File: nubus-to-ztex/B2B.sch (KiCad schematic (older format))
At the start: 14 parts, among them J1 Conn_02x07_Odd_Even, J2 Conn_01x06_Male, J8 Conn_02x07_Odd_Even

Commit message: large update
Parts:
- added C4: 100nF, Capacitor_SMD:C_0603_1608Metric, symbol Device:C
- J1: Datasheet-ALT (none) -> https://datasheet.lcsc.com/lcsc/1811051309_MOLEX-878311420_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; Notes (none) -> 87831-1419, 87831-1420, 87831-1421, 87831-1436 only change 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
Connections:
- net +3V3: now also C4.1
- net GND: now also C4.2
- net ~NMRQ_3V3: no longer JAB1.6 (J18~IO_L23N_T3_FWE_B_15)
- net fpga_to_cpld_signal_2: no longer names the net of JAB1.16 (G14~IO_L15N_T2_DQS_ADV_B_15)
- new net NMRQ: JAB1.6 (J18~IO_L23N_T3_FWE_B_15)
- no-connect marks 4 -> 5
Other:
- note added: "User LEDS"
- note added: "design use NMRQ (active high) instead"
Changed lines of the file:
@@
 F 7 "87831-1420" H 3150 7250 50  0001 C CNN "MPN"
 F 8 "https://www2.mouser.com/ProductDetail/Molex/87831-1420?qs=QtQX4uD3c2VDCL534TqpVg%3D%3D" H 3150 7250 50  0001 C CNN "URL"
+F 9 "https://datasheet.lcsc.com/lcsc/1811051309_MOLEX-878311420_C240854.pdf" H 3150 7250 50  0001 C CNN "Datasheet-ALT"
+F 10 "87831-1419, 87831-1420, 87831-1421, 87831-1436 only change plating" H 3150 7250 50  0001 C CNN "Notes"
 	1    3150 7250
 	1    0    0    -1
@@
 Text GLabel 1600 1350 0    50   Input ~ 0
 ~RQST_3V3
-Text GLabel 4100 1350 2    50   Input ~ 0
+Text GLabel 4750 650  2    50   Input ~ 0
 ~NMRQ_3V3
 Text GLabel 1600 1550 0    50   Input ~ 0
@@
 AR Path="/618E8C75/61B5DFCC" Ref="D2"  Part="1"
 F 0 "D2" H 1000 6000 50  0000 C CNN
-F 1 "RED" H 650 5900 50  0000 R CNN
+F 1 "RED" H 1050 5750 50  0000 R CNN
 F 2 "LED_SMD:LED_0805_2012Metric" H 1000 5900 50  0001 C CNN
 F 3 "https://optoelectronics.liteon.com/upload/download/DS-22-99-0150/LTST-C170KRKT.pdf" H 1000 5900 50  0001 C CNN
@@
 AR Path="/618E8C75/61B5F405" Ref="D3"  Part="1"
 F 0 "D3" H 1000 6500 50  0000 C CNN
-F 1 "RED" H 650 6400 50  0000 R CNN
+F 1 "RED" H 1050 6250 50  0000 R CNN
 F 2 "LED_SMD:LED_0805_2012Metric" H 1000 6400 50  0001 C CNN
 F 3 "https://optoelectronics.liteon.com/upload/download/DS-22-99-0150/LTST-C170KRKT.pdf" H 1000 6400 50  0001 C CNN
@@
 AR Path="/618E8C75/61B60A6F" Ref="D4"  Part="1"
 F 0 "D4" H 1000 7000 50  0000 C CNN
-F 1 "RED" H 650 6900 50  0000 R CNN
+F 1 "RED" H 1050 6750 50  0000 R CNN
 F 2 "LED_SMD:LED_0805_2012Metric" H 1000 6900 50  0001 C CNN
 F 3 "https://optoelectronics.liteon.com/upload/download/DS-22-99-0150/LTST-C170KRKT.pdf" H 1000 6900 50  0001 C CNN
@@
 AR Path="/618E8C75/61B62362" Ref="D5"  Part="1"
 F 0 "D5" H 1000 7500 50  0000 C CNN
-F 1 "RED" H 650 7400 50  0000 R CNN
+F 1 "RED" H 1050 7250 50  0000 R CNN
 F 2 "LED_SMD:LED_0805_2012Metric" H 1000 7400 50  0001 C CNN
 F 3 "https://optoelectronics.liteon.com/upload/download/DS-22-99-0150/LTST-C170KRKT.pdf" H 1000 7400 50  0001 C CNN
@@
 Text GLabel 7400 1650 0    39   Input ~ 8
 tmoen
-Text GLabel 4100 1850 2    39   Input ~ 8
-fpga_to_cpld_signal_2
 Text GLabel 1600 1750 0    39   Input ~ 8
 fpga_to_cpld_signal
+$Comp
+L Device:C C?
+U 1 1 61F08531
+P 2750 6050
+AR Path="/618F532C/61F08531" Ref="C?"  Part="1"
+AR Path="/618E8C75/61F08531" Ref="C4"  Part="1"
+F 0 "C4" H 2775 6150 50  0000 L CNN
+F 1 "100nF" H 2775 5950 50  0000 L CNN
+F 2 "Capacitor_SMD:C_0603_1608Metric" H 2788 5900 50  0001 C CNN
+F 3 "" H 2750 6050 50  0000 C CNN
+F 4 "www.yageo.com" H 2750 6050 50  0001 C CNN "MNF1_URL"
+F 5 "CC0603KRX7R8BB104" H 2750 6050 50  0001 C CNN "MPN"
+F 6 "603-CC603KRX7R8BB104" H 2750 6050 50  0001 C CNN "Mouser"
+F 7 "?" H 2750 6050 50  0001 C CNN "Digikey"
+F 8 "?" H 2750 6050 50  0001 C CNN "LCSC"
+F 9 "?" H 2750 6050 50  0001 C CNN "Koncar"
+F 10 "TB" H 2750 6050 50  0001 C CNN "Side"
+	1    2750 6050
+	1    0    0    -1
+$EndComp
+$Comp
+L power:GND #PWR0132
+U 1 1 61F08538
+P 2750 6200
+F 0 "#PWR0132" H 2750 5950 50  0001 C CNN
+F 1 "GND" H 2755 6027 50  0000 C CNN
+F 2 "" H 2750 6200 50  0001 C CNN
+F 3 "" H 2750 6200 50  0001 C CNN
+	1    2750 6200
+	1    0    0    -1
+$EndComp
+$Comp
+L power:+3.3V #PWR0133
+U 1 1 61F0853E
+P 2750 5900
+F 0 "#PWR0133" H 2750 5750 50  0001 C CNN
+F 1 "+3.3V" H 2765 6073 50  0000 C CNN
+F 2 "" H 2750 5900 50  0001 C CNN
+F 3 "" H 2750 5900 50  0001 C CNN
+	1    2750 5900
+	1    0    0    -1
+$EndComp
+Text Notes 1200 5650 0    50   ~ 0
+User LEDS
+Text GLabel 4100 1350 2    50   Input ~ 0
+NMRQ
+Text Notes 5700 550  2    50   ~ 0
+design use NMRQ (active high) instead
+NoConn ~ 4750 650
 $EndSCHEMATC

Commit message: another update after discussion on tinkerdifferent
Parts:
- removed D4, D5: RED, LED_SMD:LED_0805_2012Metric, symbol Device:LED_ALT
- removed R10, R9: 549, Resistor_SMD:R_0603_1608Metric, symbol Device:R
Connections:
- net NMRQ is gone; now on net ~NMRQ_3V3: JAB1.6 (J18~IO_L23N_T3_FWE_B_15)
- net LED2: no longer JCD1.16 (T5~IO_L12P_T1_MRCC_34)
- net LED3: no longer JCD1.18 (T4~IO_L12N_T1_MRCC_34)
- net fpga_to_cpld_signal_2: now reaches JAB1.16 (G14~IO_L15N_T2_DQS_ADV_B_15)
- new net ~CLK2X_3V3: JCD1.16 (T5~IO_L12P_T1_MRCC_34)
- new net ~TM2_3V3: JCD1.18 (T4~IO_L12N_T1_MRCC_34)
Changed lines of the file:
@@
 Text GLabel 1850 6400 2    60   Input ~ 12
 LED1
-Wire Wire Line
-	850  6900 700  6900
-Wire Wire Line
-	700  6900 700  7100
-Wire Wire Line
-	1150 6900 1550 6900
-$Comp
-L Device:R R?
-U 1 1 61B60A5F
-P 1700 6900
-AR Path="/5F6B165A/61B60A5F" Ref="R?"  Part="1"
-AR Path="/5F67E4B9/61B60A5F" Ref="R?"  Part="1"
-AR Path="/618E8C75/61B60A5F" Ref="R9"  Part="1"
-F 0 "R9" V 1780 6900 50  0000 C CNN
-F 1 "549" V 1700 6900 50  0000 C CNN
-F 2 "Resistor_SMD:R_0603_1608Metric" V 1630 6900 50  0001 C CNN
-F 3 "" H 1700 6900 50  0000 C CNN
-F 4 "0603WAF5490T5E" V 1700 6900 50  0001 C CNN "MPN"
-F 5 "https://lcsc.com/product-detail/Chip-Resistor-Surface-Mount_UNI-ROYAL-Uniroyal-Elec-0603WAF5490T5E_C23079.html" V 1700 6900 50  0001 C CNN "URL"
-	1    1700 6900
-	0    1    1    0
-$EndComp
-$Comp
-L Device:LED_ALT D?
-U 1 1 61B60A6F
-P 1000 6900
-AR Path="/5F6B165A/61B60A6F" Ref="D?"  Part="1"
-AR Path="/5F67E4B9/61B60A6F" Ref="D?"  Part="1"
-AR Path="/618E8C75/61B60A6F" Ref="D4"  Part="1"
-F 0 "D4" H 1000 7000 50  0000 C CNN
-F 1 "RED" H 1050 6750 50  0000 R CNN
-F 2 "LED_SMD:LED_0805_2012Metric" H 1000 6900 50  0001 C CNN
-F 3 "https://optoelectronics.liteon.com/upload/download/DS-22-99-0150/LTST-C170KRKT.pdf" H 1000 6900 50  0001 C CNN
-F 4 "www.liteon.com" H 1000 6900 60  0001 C CNN "MNF1_URL"
-F 5 "LTST-C170KRKT" H 1000 6900 60  0001 C CNN "MPN"
-F 6 "https://www.lcsc.com/product-detail/Light-Emitting-Diodes-LED_Lite-On-LTST-C170KRKT_C94868.html" H 1000 6900 50  0001 C CNN "URL"
-	1    1000 6900
-	1    0    0    -1
-$EndComp
-$Comp
-L power:GND #PWR0177
-U 1 1 61B60A76
-P 700 7100
-F 0 "#PWR0177" H 700 6850 50  0001 C CNN
-F 1 "GND" H 705 6927 50  0000 C CNN
-F 2 "" H 700 7100 50  0001 C CNN
-F 3 "" H 700 7100 50  0001 C CNN
-	1    700  7100
-	1    0    0    -1
-$EndComp
-Text GLabel 1850 6900 2    60   Input ~ 12
-LED2
-Wire Wire Line
-	850  7400 700  7400
-Wire Wire Line
-	700  7400 700  7600
-Wire Wire Line
-	1150 7400 1550 7400
-$Comp
-L Device:R R?
-U 1 1 61B62352
-P 1700 7400
-AR Path="/5F6B165A/61B62352" Ref="R?"  Part="1"
-AR Path="/5F67E4B9/61B62352" Ref="R?"  Part="1"
-AR Path="/618E8C75/61B62352" Ref="R10"  Part="1"
-F 0 "R10" V 1780 7400 50  0000 C CNN
-F 1 "549" V 1700 7400 50  0000 C CNN
-F 2 "Resistor_SMD:R_0603_1608Metric" V 1630 7400 50  0001 C CNN
-F 3 "" H 1700 7400 50  0000 C CNN
-F 4 "0603WAF5490T5E" V 1700 7400 50  0001 C CNN "MPN"
-F 5 "https://lcsc.com/product-detail/Chip-Resistor-Surface-Mount_UNI-ROYAL-Uniroyal-Elec-0603WAF5490T5E_C23079.html" V 1700 7400 50  0001 C CNN "URL"
-	1    1700 7400
-	0    1    1    0
-$EndComp
-$Comp
-L Device:LED_ALT D?
-U 1 1 61B62362
-P 1000 7400
-AR Path="/5F6B165A/61B62362" Ref="D?"  Part="1"
-AR Path="/5F67E4B9/61B62362" Ref="D?"  Part="1"
-AR Path="/618E8C75/61B62362" Ref="D5"  Part="1"
-F 0 "D5" H 1000 7500 50  0000 C CNN
-F 1 "RED" H 1050 7250 50  0000 R CNN
-F 2 "LED_SMD:LED_0805_2012Metric" H 1000 7400 50  0001 C CNN
-F 3 "https://optoelectronics.liteon.com/upload/download/DS-22-99-0150/LTST-C170KRKT.pdf" H 1000 7400 50  0001 C CNN
-F 4 "www.liteon.com" H 1000 7400 60  0001 C CNN "MNF1_URL"
-F 5 "LTST-C170KRKT" H 1000 7400 60  0001 C CNN "MPN"
-F 6 "https://www.lcsc.com/product-detail/Light-Emitting-Diodes-LED_Lite-On-LTST-C170KRKT_C94868.html" H 1000 7400 50  0001 C CNN "URL"
-	1    1000 7400
-	1    0    0    -1
-$EndComp
-$Comp
-L power:GND #PWR0178
-U 1 1 61B62369
-P 700 7600
-F 0 "#PWR0178" H 700 7350 50  0001 C CNN
-F 1 "GND" H 705 7427 50  0000 C CNN
-F 2 "" H 700 7600 50  0001 C CNN
-F 3 "" H 700 7600 50  0001 C CNN
-	1    700  7600
-	1    0    0    -1
-$EndComp
-Text GLabel 1850 7400 2    60   Input ~ 12
-LED3
 Text GLabel 9900 1650 2    60   Input ~ 12
 LED0
 Text GLabel 9900 1750 2    60   Input ~ 12
 LED1
-Text GLabel 9900 1850 2    60   Input ~ 12
-LED2
-Text GLabel 9900 1950 2    60   Input ~ 12
-LED3
 Text GLabel 1600 4050 0    50   Input ~ 0
 USBH0_D+
@@
 User LEDS
 Text GLabel 4100 1350 2    50   Input ~ 0
-NMRQ
+~NMRQ_3V3
 Text Notes 5700 550  2    50   ~ 0
 design use NMRQ (active high) instead
 NoConn ~ 4750 650
+Text GLabel 4100 1850 2    39   Input ~ 8
+fpga_to_cpld_signal_2
+Text GLabel 12450 1800 2    60   Input ~ 12
+LED3
+Text GLabel 12450 1700 2    60   Input ~ 12
+LED2
+Text GLabel 9900 1950 2    50   Input ~ 0
+~TM2_3V3
+Text GLabel 9900 1850 2    50   Input ~ 0
+~CLK2X_3V3
 $EndSCHEMATC

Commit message: large clean-up update
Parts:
- added C3: 47uF 10V+, Capacitor_SMD:C_0805_2012Metric, symbol Device:C
- added D3: BLUE, LED_SMD:LED_0805_2012Metric, symbol Device:LED_ALT
- added R3: 549, Resistor_SMD:R_0603_1608Metric, symbol Device:R
- renumbered C19 to C1, C4 to C2, D2 to D1, D3 to D2, J8 to J2, J2 to J3, R7 to R1, R8 to R2
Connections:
- net +3V3: now also R3.1
- net +5V: now also C3.1
- net GND: now also C3.2, D3.1 (K)
- new net: D3.2 (A), R3.2
- no-connect marks 5 -> 4
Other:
- note added: "Close to VIN\npins on AB"
- note added: "Close to pwr output pins\n(3.3V / VCCO_{AB,CD})"
- note added: "Power Signal"
- note added: "Serial port-like header\n(just two signals & gnd, really)"
- note removed: "design use NMRQ (active high) instead"
- moved on the sheet: C1, C2

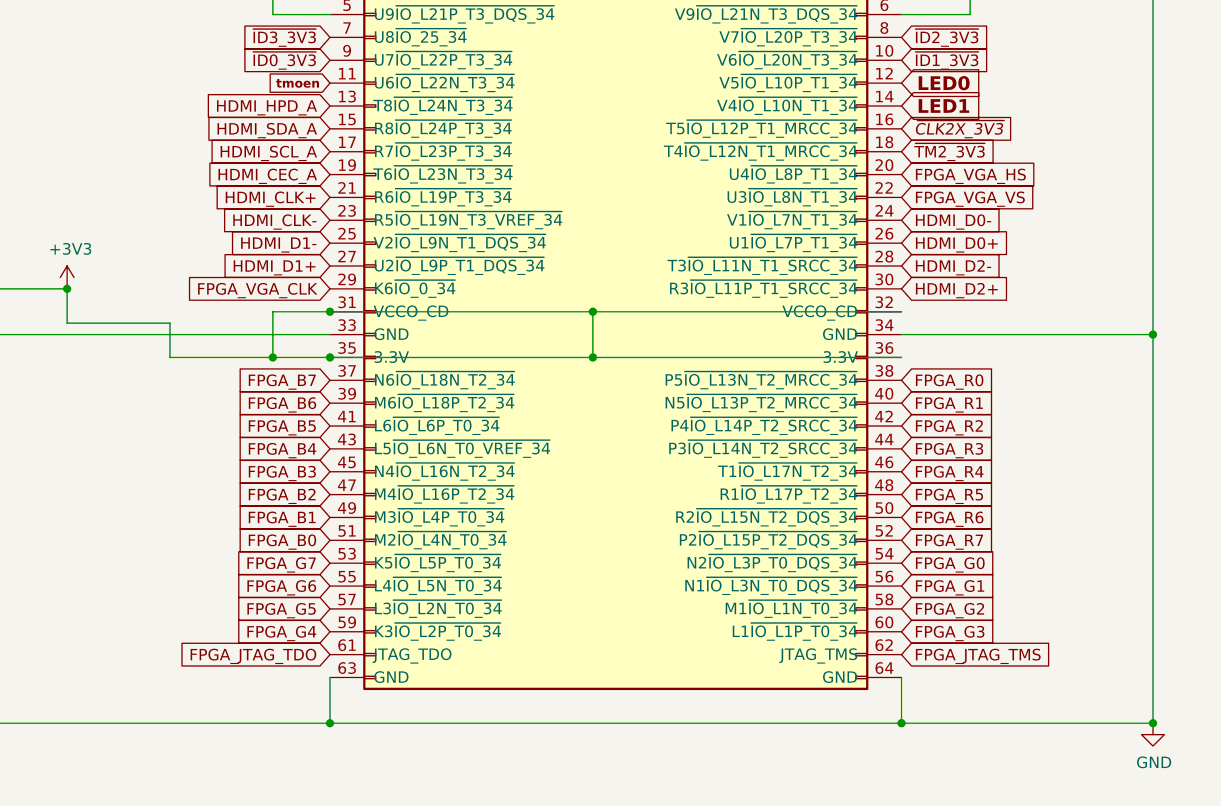
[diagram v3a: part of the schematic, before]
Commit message: drop vga
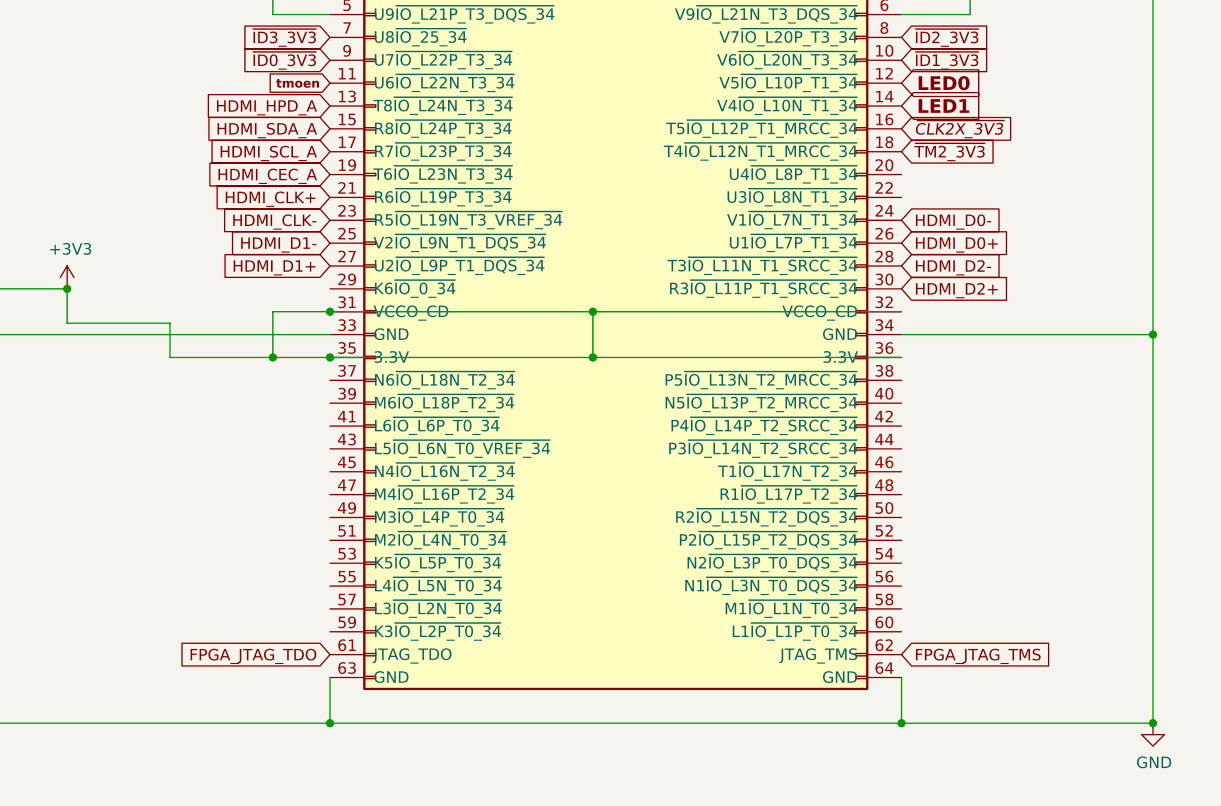
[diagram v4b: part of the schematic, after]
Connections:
- net FPGA_B0: no longer names the net of JCD1.51 (M2~IO_L4N_T0_34)
- net FPGA_B1: no longer names the net of JCD1.49 (M3~IO_L4P_T0_34)
- net FPGA_B2: no longer names the net of JCD1.47 (M4~IO_L16P_T2_34)
- net FPGA_B3: no longer names the net of JCD1.45 (N4~IO_L16N_T2_34)
- net FPGA_B4: no longer names the net of JCD1.43 (L5~IO_L6N_T0_VREF_34)
- net FPGA_B5: no longer names the net of JCD1.41 (L6~IO_L6P_T0_34)
- net FPGA_B6: no longer names the net of JCD1.39 (M6~IO_L18P_T2_34)
- net FPGA_B7: no longer names the net of JCD1.37 (N6~IO_L18N_T2_34)
- net FPGA_G0: no longer names the net of JCD1.54 (N2~IO_L3P_T0_DQS_34)
- net FPGA_G1: no longer names the net of JCD1.56 (N1~IO_L3N_T0_DQS_34)
- net FPGA_G2: no longer names the net of JCD1.58 (M1~IO_L1N_T0_34)
- net FPGA_G3: no longer names the net of JCD1.60 (L1~IO_L1P_T0_34)
- net FPGA_G4: no longer names the net of JCD1.59 (K3~IO_L2P_T0_34)
- net FPGA_G5: no longer names the net of JCD1.57 (L3~IO_L2N_T0_34)
- net FPGA_G6: no longer names the net of JCD1.55 (L4~IO_L5N_T0_34)
- net FPGA_G7: no longer names the net of JCD1.53 (K5~IO_L5P_T0_34)
- net FPGA_R0: no longer names the net of JCD1.38 (P5~IO_L13N_T2_MRCC_34)
- net FPGA_R1: no longer names the net of JCD1.40 (N5~IO_L13P_T2_MRCC_34)
- net FPGA_R2: no longer names the net of JCD1.42 (P4~IO_L14P_T2_SRCC_34)
- net FPGA_R3: no longer names the net of JCD1.44 (P3~IO_L14N_T2_SRCC_34)
- net FPGA_R4: no longer names the net of JCD1.46 (T1~IO_L17N_T2_34)
- net FPGA_R5: no longer names the net of JCD1.48 (R1~IO_L17P_T2_34)
- net FPGA_R6: no longer names the net of JCD1.50 (R2~IO_L15N_T2_DQS_34)
- net FPGA_R7: no longer names the net of JCD1.52 (P2~IO_L15P_T2_DQS_34)
- net FPGA_VGA_CLK: no longer names the net of JCD1.29 (K6~IO_0_34)
- net FPGA_VGA_HS: no longer names the net of JCD1.20 (U4~IO_L8P_T1_34)
- net FPGA_VGA_VS: no longer names the net of JCD1.22 (U3~IO_L8N_T1_34)
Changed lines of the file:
@@
 Text GLabel 1600 2450 0    39   Input ~ 8
 NUBUS_OE
-Text GLabel 9900 2950 2    50   Input ~ 0
-FPGA_R0
-Text GLabel 9900 3050 2    50   Input ~ 0
-FPGA_R1
-Text GLabel 9900 3150 2    50   Input ~ 0
-FPGA_R2
-Text GLabel 9900 3250 2    50   Input ~ 0
-FPGA_R3
-Text GLabel 9900 3350 2    50   Input ~ 0
-FPGA_R4
-Text GLabel 9900 3450 2    50   Input ~ 0
-FPGA_R5
-Text GLabel 9900 3550 2    50   Input ~ 0
-FPGA_R6
-Text GLabel 9900 3650 2    50   Input ~ 0
-FPGA_R7
-Text GLabel 9900 3750 2    50   Input ~ 0
-FPGA_G0
-Text GLabel 9900 3850 2    50   Input ~ 0
-FPGA_G1
-Text GLabel 9900 3950 2    50   Input ~ 0
-FPGA_G2
-Text GLabel 9900 4050 2    50   Input ~ 0
-FPGA_G3
-Text GLabel 7400 4050 0    50   Input ~ 0
-FPGA_G4
-Text GLabel 7400 3950 0    50   Input ~ 0
-FPGA_G5
-Text GLabel 7400 3850 0    50   Input ~ 0
-FPGA_G6
-Text GLabel 7400 3750 0    50   Input ~ 0
-FPGA_G7
-Text GLabel 7400 3650 0    50   Input ~ 0
-FPGA_B0
-Text GLabel 7400 3550 0    50   Input ~ 0
-FPGA_B1
-Text GLabel 7400 3450 0    50   Input ~ 0
-FPGA_B2
-Text GLabel 7400 3350 0    50   Input ~ 0
-FPGA_B3
-Text GLabel 7400 3250 0    50   Input ~ 0
-FPGA_B4
-Text GLabel 7400 3150 0    50   Input ~ 0
-FPGA_B5
-Text GLabel 7400 3050 0    50   Input ~ 0
-FPGA_B6
-Text GLabel 7400 2950 0    50   Input ~ 0
-FPGA_B7
-Text GLabel 7400 2550 0    50   Input ~ 0
-FPGA_VGA_CLK
-Text GLabel 9900 2050 2    50   Input ~ 0
-FPGA_VGA_HS
-Text GLabel 9900 2150 2    50   Input ~ 0
-FPGA_VGA_VS
 Wire Wire Line
 	11000 1250 11000 2750

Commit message: forgot to commit last attempt at V1.2
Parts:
- removed J2: Conn_02x07_Odd_Even, For_SeeedStudio:PinHeader_2x07_P2.00mm_Vertical_For_SeeedStudio, symbol Connector_Generic:Conn_02x07_Odd_Even
- added D4, D5: RED, LED_SMD:LED_0805_2012Metric, symbol Device:LED_ALT
- added R10, R9: 549, Resistor_SMD:R_0603_1608Metric, symbol Device:R
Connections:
- net GND: now also D4.1 (K), D5.1 (K)
- net HDMI_CEC_A: now also JCD1.43 (L5~IO_L6N_T0_VREF_34); no longer JCD1.19 (T6~IO_L23N_T3_34)
- net HDMI_CLK+: now also JCD1.47 (M4~IO_L16P_T2_34); no longer JCD1.21 (R6~IO_L19P_T3_34)
- net HDMI_CLK-: now also JCD1.45 (N4~IO_L16N_T2_34); no longer JCD1.23 (R5~IO_L19N_T3_VREF_34)
- net HDMI_D0+: now also JCD1.49 (M3~IO_L4P_T0_34); no longer JCD1.26 (U1~IO_L7P_T1_34)
- net HDMI_D0-: now also JCD1.51 (M2~IO_L4N_T0_34); no longer JCD1.24 (V1~IO_L7N_T1_34)
- net HDMI_D1+: now also JCD1.53 (K5~IO_L5P_T0_34); no longer JCD1.27 (U2~IO_L9P_T1_DQS_34)
- net HDMI_D1-: now also JCD1.55 (L4~IO_L5N_T0_34); no longer JCD1.25 (V2~IO_L9N_T1_DQS_34)
- net HDMI_D2+: now also JCD1.59 (K3~IO_L2P_T0_34); no longer JCD1.30 (R3~IO_L11P_T1_SRCC_34)
- net HDMI_D2-: now also JCD1.57 (L3~IO_L2N_T0_34); no longer JCD1.28 (T3~IO_L11N_T1_SRCC_34)
- net HDMI_HPD_A: now also JCD1.37 (N6~IO_L18N_T2_34); no longer JCD1.13 (T8~IO_L24N_T3_34)
- net HDMI_SCL_A: now also JCD1.41 (L6~IO_L6P_T0_34); no longer JCD1.17 (R7~IO_L23P_T3_34)
- net HDMI_SDA_A: now also JCD1.39 (M6~IO_L18P_T2_34); no longer JCD1.15 (R8~IO_L24P_T3_34)
- net LED0: now also JCD1.54 (N2~IO_L3P_T0_DQS_34); no longer JCD1.12 (V5~IO_L10P_T1_34)
- net LED1: now also JCD1.56 (N1~IO_L3N_T0_DQS_34); no longer JCD1.14 (V4~IO_L10N_T1_34)
- net NUBUS_AD_DIR: now also JAB1.17 (G17~IO_L18N_T2_A23_15); no longer JAB1.18 (G16~IO_L13N_T2_MRCC_15)
- net ~ACK_3V3: now also JAB1.8 (J17~IO_L23P_T3_FOE_B_15); no longer JAB1.10 (K13~IO_L17P_T2_A26_15)
- net ~RESET_3V3: now also JCD1.52 (P2~IO_L15P_T2_DQS_34); no longer JAB1.17 (G17~IO_L18N_T2_A23_15)
- net ~START_3V3: now also JAB1.7 (K15~IO_L24P_T3_RS1_15); no longer JAB1.9 (J15~IO_L24N_T3_RS0_15)
- net ~TM0_3V3: now also JCD1.38 (P5~IO_L13N_T2_MRCC_34); no longer JAB1.7 (K15~IO_L24P_T3_RS1_15)
- net ~TM1_3V3: now also JCD1.40 (N5~IO_L13P_T2_MRCC_34); no longer JAB1.8 (J17~IO_L23P_T3_FOE_B_15)
- net ~TM2_3V3: now also JCD1.50 (R2~IO_L15N_T2_DQS_34); no longer JCD1.18 (T4~IO_L12N_T1_MRCC_34)
- net SD_D0: now reaches JCD1.20 (U4~IO_L8P_T1_34)
- net SD_CLK: now reaches JCD1.22 (U3~IO_L8N_T1_34)
- net PMOD-11: now reaches JCD1.29 (K6~IO_0_34)
- net TM1_n_o: now reaches JCD1.42 (P4~IO_L14P_T2_SRCC_34)
- net TM0_n_o: now reaches JCD1.44 (P3~IO_L14N_T2_SRCC_34)
- net TM2_oe_n: now reaches JCD1.46 (T1~IO_L17N_T2_34)
- net TM2_o_n: now reaches JCD1.48 (R1~IO_L17P_T2_34)
- net LED2: now reaches JCD1.58 (M1~IO_L1N_T0_34)
- net LED2: now also R9.1
- net LED3: now reaches JCD1.60 (L1~IO_L1P_T0_34)
- net LED3: now also R10.1
- net ARB renamed ACK_oe_n
- net GRANT renamed START_o_n
- net NUBUS_MASTER_DIR renamed ARB3_o_n
- net fpga_to_cpld_clk renamed ACK_o_n
- net fpga_to_cpld_signal renamed ARB0_o_n
- net fpga_to_cpld_signal_2 renamed ARB2_o_n
- net tmoen renamed ~ARB3_3V3
- new net: D4.2 (A), R9.2
- new net: D5.2 (A), R10.2
- new net ARB1_o_n: JAB1.18 (G16~IO_L13N_T2_MRCC_15)
- new net PMOD-10: JCD1.23 (R5~IO_L19N_T3_VREF_34)
- new net PMOD-12: JCD1.27 (U2~IO_L9P_T1_DQS_34)
- new net PMOD-5: JCD1.17 (R7~IO_L23P_T3_34)
- new net PMOD-6: JCD1.15 (R8~IO_L24P_T3_34)
- new net PMOD-7: JCD1.21 (R6~IO_L19P_T3_34)
- new net PMOD-8: JCD1.19 (T6~IO_L23N_T3_34)
- new net PMOD-9: JCD1.25 (V2~IO_L9N_T1_DQS_34)
- new net RQST_o_n: JAB1.10 (K13~IO_L17P_T2_A26_15)
- new net SD_CMD: JCD1.24 (V1~IO_L7N_T1_34)
- new net SD_D1: JCD1.18 (T4~IO_L12N_T1_MRCC_34)
- new net SD_D2: JCD1.28 (T3~IO_L11N_T1_SRCC_34)
- new net SD_D3: JCD1.26 (U1~IO_L7P_T1_34)
- new net START_oe_n: JAB1.9 (J15~IO_L24N_T3_RS0_15)
- new net TMx_oe_n: JCD1.30 (R3~IO_L11P_T1_SRCC_34)
- new net ~ARB0_3V3: JCD1.13 (T8~IO_L24N_T3_34)
- new net ~ARB1_3V3: JCD1.14 (V4~IO_L10N_T1_34)
- new net ~ARB2_3V3: JCD1.12 (V5~IO_L10P_T1_34)
- no-connect marks 4 -> 2

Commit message: cleanups, alternative MPN for 2x32 headers (TBC)
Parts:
- JAB1, JCD1: MPN 10-89-7642 -> X6521WV-2x32H-C30D60; MPN-ALT (none) -> 10-89-7642
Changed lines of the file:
@@
 F 2 "For_SeeedStudio:PinHeader_2x32_P2.54mm_Vertical_For_SeeedStudio" H 1800 2650 50  0001 C CNN
 F 3 "" H 1800 2650 50  0001 C CNN
-F 4 "10-89-7642" H 1800 2650 50  0001 C CNN "MPN"
+F 4 "10-89-7642" H 1800 2650 50  0001 C CNN "MPN-ALT"
 F 5 "https://www2.mouser.com/ProductDetail/Molex/10-89-7642?qs=%2Fha2pyFadugCxzQFZUdvioDcljDVidgd4vXrOFuSRYM%3D" H 1800 2650 50  0001 C CNN "URL"
+F 6 "X6521WV-2x32H-C30D60" H 1800 2650 50  0001 C CNN "MPN"
 	1    1800 2650
 	1    0    0    -1
@@
 F 2 "For_SeeedStudio:PinHeader_2x32_P2.54mm_Vertical_For_SeeedStudio" H 7600 2650 50  0001 C CNN
 F 3 "" H 7600 2650 50  0001 C CNN
-F 4 "10-89-7642" H 7600 2650 50  0001 C CNN "MPN"
+F 4 "10-89-7642" H 7600 2650 50  0001 C CNN "MPN-ALT"
 F 5 "https://www2.mouser.com/ProductDetail/Molex/10-89-7642?qs=%2Fha2pyFadugCxzQFZUdvioDcljDVidgd4vXrOFuSRYM%3D" H 7600 2650 50  0001 C CNN "URL"
+F 6 "X6521WV-2x32H-C30D60" H 7600 2650 50  0001 C CNN "MPN"
 	1    7600 2650
 	1    0    0    -1
